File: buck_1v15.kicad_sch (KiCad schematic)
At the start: 20 parts, among them U2 TPS564257DRLR

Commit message: switch: buck v1.1 -> v1.15 as requested by the switch
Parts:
- renumbered C80 to C?, C72 to C?, C76 to C?, C73 to C?, C75 to C?, C71 to C?, C26 to C?, C79 to C?, C70 to C?, L2 to L?, R15 to R?, R84 to R?, R82 to R?, R16 to R?, R79 to R?, TP1 to TP?, TP10 to TP?, TP11 to TP?, TP3 to TP?, U2 to U?

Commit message: This commit intends to fix multiple issues:
 - 1.1 -> 1.15 v buck rails
 - Revision consistently using Rev. A
 - Issue with the Switch symbol when moving library
 - Adding new footprint and symbol for 2.54mm Headers
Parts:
- gave numbers to parts that had none: 20
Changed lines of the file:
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@@
 		(dnp no)
 		(fields_autoplaced yes)
-		(property "Reference" "#PWR?"
+		(property "Reference" "#PWR011"
 			(at 219.71 77.47 0)
 			(effects
@@
 		(dnp no)
 		(fields_autoplaced yes)
-		(property "Reference" "#PWR?"
+		(property "Reference" "#PWR015"
 			(at 85.09 107.95 0)
 			(effects
@@
 		(dnp no)
 		(fields_autoplaced yes)
-		(property "Reference" "TP?"
+		(property "Reference" "TP1"
 			(at 232.41 57.785 0)
 			(do_not_autoplace yes)
@@
 		(dnp yes)
 		(fields_autoplaced yes)
-		(property "Reference" "C?"
+		(property "Reference" "C80"
 			(at 88.9 92.7099 0)
 			(effects
@@
 		(on_board yes)
 		(dnp no)
-		(property "Reference" "R?"
+		(property "Reference" "R15"
 			(at 170.18 52.324 90)
 			(effects
@@
 		(dnp no)
 		(fields_autoplaced yes)
-		(property "Reference" "TP?"
+		(property "Reference" "TP10"
 			(at 166.624 67.31 90)
 			(do_not_autoplace yes)
@@
 		(dnp no)
 		(fields_autoplaced yes)
-		(property "Reference" "C?"
+		(property "Reference" "C72"
 			(at 241.3 66.0399 0)
 			(effects
@@
 		(dnp no)
 		(fields_autoplaced yes)
-		(property "Reference" "C?"
+		(property "Reference" "C76"
 			(at 93.98 72.3899 0)
 			(effects
@@
 		(dnp yes)
 		(fields_autoplaced yes)
-		(property "Reference" "C?"
+		(property "Reference" "C73"
 			(at 180.34 67.3099 0)
 			(effects
@@
 		(dnp yes)
 		(fields_autoplaced yes)
-		(property "Reference" "C?"
+		(property "Reference" "C75"
 			(at 82.55 72.3899 0)
 			(effects
@@
 		(dnp no)
 		(fields_autoplaced yes)
-		(property "Reference" "L?"
+		(property "Reference" "L2"
 			(at 170.18 61.722 0)
 			(do_not_autoplace yes)
@@
 		(dnp yes)
 		(fields_autoplaced yes)
-		(property "Reference" "R?"
+		(property "Reference" "R84"
 			(at 99.06 92.7099 0)
 			(effects
@@
 		(dnp no)
 		(fields_autoplaced yes)
-		(property "Reference" "R?"
+		(property "Reference" "R82"
 			(at 190.5 81.2799 0)
 			(effects
@@
 		(dnp no)
 		(fields_autoplaced yes)
-		(property "Reference" "C?"
+		(property "Reference" "C71"
 			(at 229.87 66.0399 0)
 			(effects
@@
 		(dnp yes)
 		(fields_autoplaced yes)
-		(property "Reference" "C?"
+		(property "Reference" "C26"
 			(at 207.01 66.0399 0)
 			(effects
@@
 		(dnp no)
 		(fields_autoplaced yes)
-		(property "Reference" "C?"
+		(property "Reference" "C79"
 			(at 105.41 72.3899 0)
 			(effects
@@
 		(on_board yes)
 		(dnp no)
-		(property "Reference" "R?"
+		(property "Reference" "R16"
 			(at 64.77 63.5 90)
 			(effects
@@
 		(dnp no)
 		(fields_autoplaced yes)
-		(property "Reference" "R?"
+		(property "Reference" "R79"
 			(at 190.5 67.3099 0)
 			(effects
@@
 		(dnp no)
 		(fields_autoplaced yes)
-		(property "Reference" "#PWR?"
+		(property "Reference" "#PWR014"
 			(at 187.96 96.52 0)
 			(effects
@@
 		(dnp no)
 		(fields_autoplaced yes)
-		(property "Reference" "TP?"
+		(property "Reference" "TP11"
 			(at 96.52 84.455 0)
 			(do_not_autoplace yes)
@@
 		(dnp no)
 		(fields_autoplaced yes)
-		(property "Reference" "#PWR?"
+		(property "Reference" "#PWR010"
 			(at 214.63 64.77 0)
 			(effects
@@
 		(dnp no)
 		(fields_autoplaced yes)
-		(property "Reference" "#PWR?"
+		(property "Reference" "#PWR012"
 			(at 154.94 82.55 0)
 			(effects
@@
 		(dnp no)
 		(fields_autoplaced yes)
-		(property "Reference" "C?"
+		(property "Reference" "C70"
 			(at 218.44 66.0399 0)
 			(effects
@@
 		(dnp no)
 		(fields_autoplaced yes)
-		(property "Reference" "TP?"
+		(property "Reference" "TP3"
 			(at 71.12 60.325 0)
 			(do_not_autoplace yes)
@@
 		(dnp no)
 		(fields_autoplaced yes)
-		(property "Reference" "#PWR?"
+		(property "Reference" "#PWR013"
 			(at 90.17 85.09 0)
 			(effects
@@
 		(dnp no)
 		(fields_autoplaced yes)
-		(property "Reference" "#PWR?"
+		(property "Reference" "#PWR023"
 			(at 48.26 53.34 0)
 			(effects
@@
 		(dnp no)
 		(fields_autoplaced yes)
-		(property "Reference" "U?"
+		(property "Reference" "U2"
 			(at 134.62 55.88 0)
 			(effects
@@
 		(dnp no)
 		(fields_autoplaced yes)
-		(property "Reference" "#PWR?"
+		(property "Reference" "#PWR022"
 			(at 48.26 38.1 0)
 			(effects

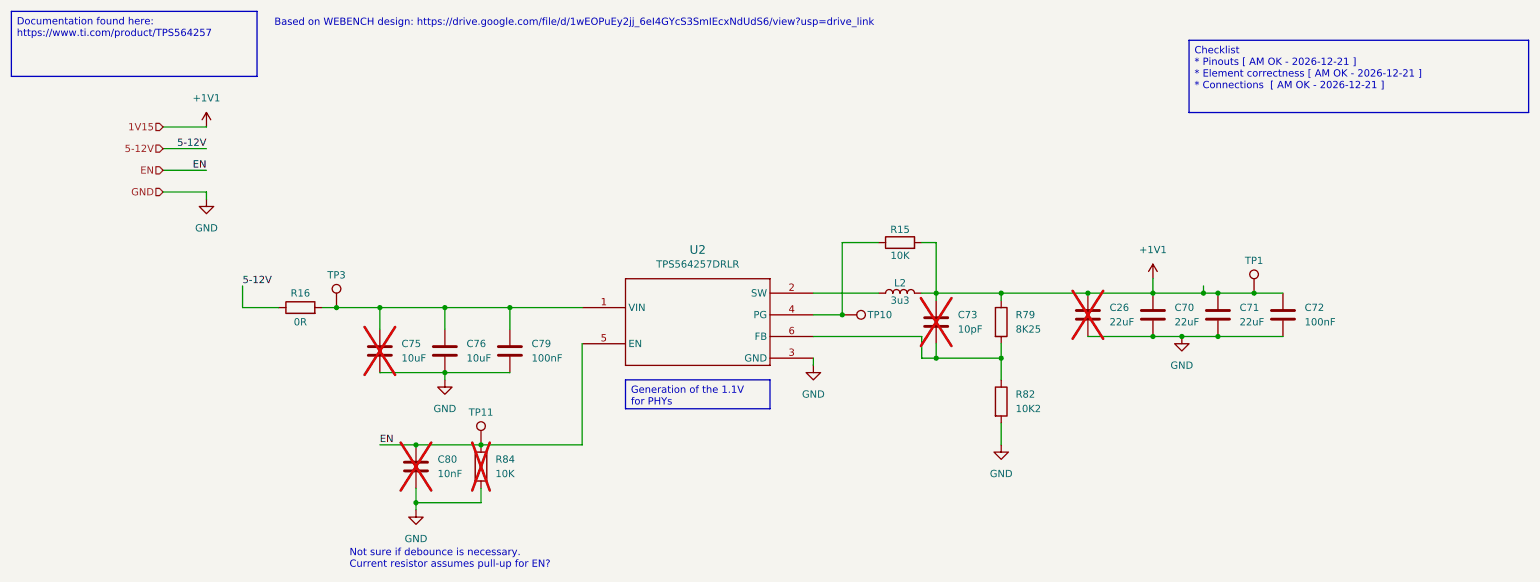
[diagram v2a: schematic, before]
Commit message: fixing issue related to symbol changes, and updating components
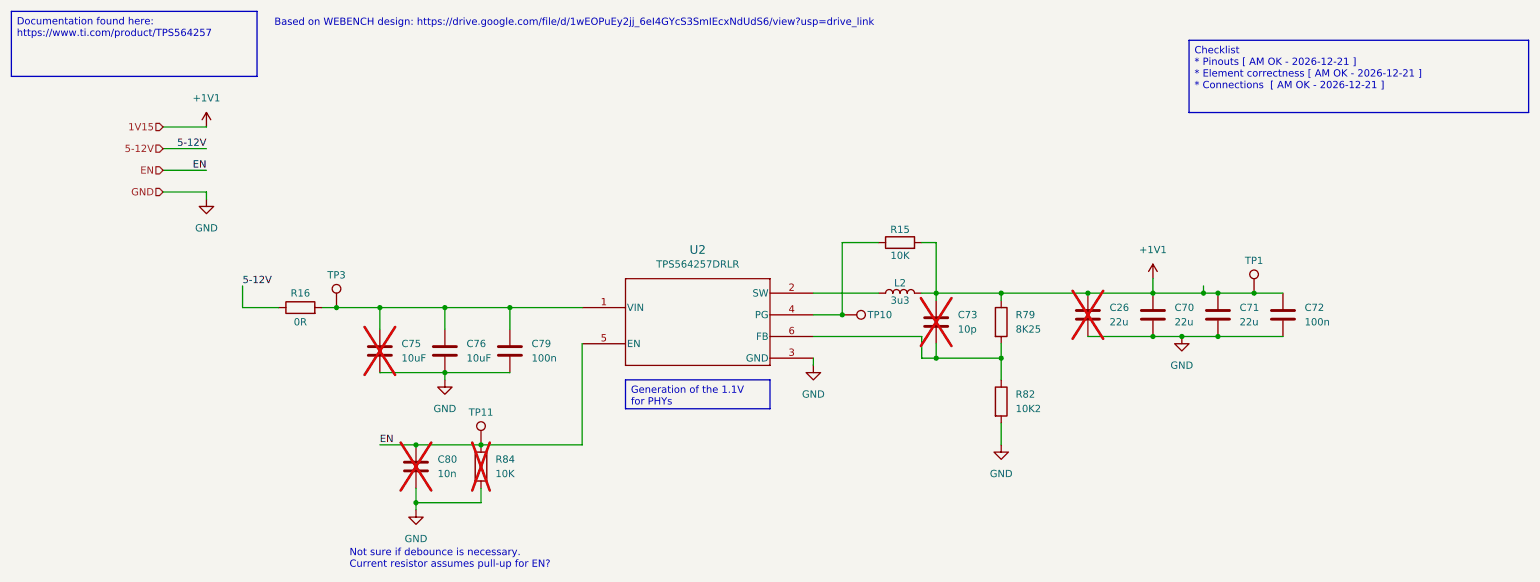
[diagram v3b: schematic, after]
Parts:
- C26, C70, C71: value 22uF -> 22u; symbol KL_C:C_22uF_10V_X5R_0603_20 -> KL_C:C_22u_10V_X5R_0603_20; Digikey 490-10476-1-ND -> 490-13243-1-ND; LCSC C84419 -> C361061; Mouser 81-GRM188R61A226ME5D -> 81-GRM187R61A226ME5D
- C72: value 100nF -> 100n; footprint KL:C_0603 -> Capacitor_SMD:C_0201_0603Metric; symbol KL_C:C_100nF_10V_X7R_0603_10 -> KL_C:C_100n_10V_X7R_0603_10
- C73: value 10pF -> 10p; symbol KL_C:C_10pF_25V_C0G_0603_5 -> KL_C:C_10p_25V_C0G_0603_5
- C75, C76: footprint KL:C_0603 -> Capacitor_SMD:C_0201_0603Metric; symbol KL_C:C_10uF_25V_X5R_0603_20 -> KL_C:C_10u_25V_X5R_0603_20
- C79: value 100nF -> 100n; footprint KL:C_0603 -> Capacitor_SMD:C_0201_0603Metric; symbol KL_C:C_100nF_16V_X7R_0603_10 -> KL_C:C_100n_16V_X7R_0603_10
- C80: value 10nF -> 10n; footprint KL:C_0603 -> Capacitor_SMD:C_0201_0603Metric; symbol KL_C:C_10nF_25V_X7R_0603_20 -> KL_C:C_10n_50V_X7R_0603_10; Digikey 311-3111-1-ND -> 1276-CL10B103KB8WPNDCT-ND; LCSC C726559 -> C307346; Mouser 603-AC603KRX7R8BB103 -> 187-CL10B103KB8WPND; Tolerance 20 -> 10; Voltage 25 -> 50; now in the parts list
- R82, R84: footprint KL:R_0603 -> KL_Footprints:C_0603
- U2: footprint KL:SOT-563 -> KL_Footprints:SOT-563; symbol KL_IC_Power:TI_TPS564357DRLR -> KL_Voltage_Regulators:TPS564257DRLR; LCSC (none) -> C19272233; Mouser 595-TPS564257DRLR -> 595-TPS564257DRLR
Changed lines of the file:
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@@
 		(dnp no)
 		(fields_autoplaced yes)
-		(property "Reference" "#PWR011"
+		(property "Reference" "#PWR11"
 			(at 219.71 77.47 0)
 			(effects
@@
 			(project "shish-lan"
 				(path "/d4536448-b109-4159-96e2-3dc21baf2d6e/0b7d9af9-83c1-43fa-a7a0-a33d0a00ea9c/42c65065-b6e5-43b0-ae2c-34333f058269"
-					(reference "#PWR011")
+					(reference "#PWR11")
 					(unit 1)
 				)
@@
 		(dnp no)
 		(fields_autoplaced yes)
-		(property "Reference" "#PWR015"
+		(property "Reference" "#PWR15"
 			(at 85.09 107.95 0)
 			(effects
@@
 			(project "shish-lan"
 				(path "/d4536448-b109-4159-96e2-3dc21baf2d6e/0b7d9af9-83c1-43fa-a7a0-a33d0a00ea9c/42c65065-b6e5-43b0-ae2c-34333f058269"
-					(reference "#PWR015")
+					(reference "#PWR15")
 					(unit 1)
 				)
@@
 	)
 	(symbol
-		(lib_id "KL_C:C_10nF_25V_X7R_0603_20")
+		(lib_id "KL_C:C_10n_50V_X7R_0603_10")
 		(at 85.09 93.98 0)
 		(unit 1)
 		(exclude_from_sim no)
-		(in_bom no)
+		(in_bom yes)
 		(on_board yes)
 		(dnp yes)
@@
 			)
 		)
-		(property "Value" "10nF"
+		(property "Value" "10n"
 			(at 88.9 95.2499 0)
 			(effects
@@
 			)
 		)
-		(property "Footprint" "KL:C_0603"
+		(property "Footprint" "Capacitor_SMD:C_0201_0603Metric"
 			(at 86.0552 97.79 0)
 			(effects
@@
 			)
 		)
-		(property "Tolerance" "20"
+		(property "Tolerance" "10"
 			(at 85.09 93.98 0)
 			(effects
@@
 			)
 		)
-		(property "Voltage" "25"
+		(property "Voltage" "50"
 			(at 85.09 93.98 0)
 			(effects
@@
 			)
 		)
-		(property "Mouser" "603-AC603KRX7R8BB103"
+		(property "Mouser" "187-CL10B103KB8WPND"
 			(at 85.09 93.98 0)
 			(effects
@@
 			)
 		)
-		(property "Digikey" "311-3111-1-ND"
+		(property "Digikey" "1276-CL10B103KB8WPNDCT-ND"
 			(at 85.09 93.98 0)
 			(effects
@@
 			)
 		)
-		(property "LCSC" "C726559"
+		(property "LCSC" "C307346"
 			(at 85.09 93.98 0)
 			(effects
@@
 	)
 	(symbol
-		(lib_name "R_10K_100mW_5_0603_1")
 		(lib_id "KL_R:R_10K_100mW_5_0603")
 		(at 170.18 54.61 90)
@@
 	)
 	(symbol
-		(lib_id "KL_C:C_100nF_10V_X7R_0603_10")
+		(lib_id "KL_C:C_100n_10V_X7R_0603_10")
 		(at 237.49 67.31 0)
 		(unit 1)
@@
 			)
 		)
-		(property "Value" "100nF"
+		(property "Value" "100n"
 			(at 241.3 68.5799 0)
 			(effects
@@
 			)
 		)
-		(property "Footprint" "KL:C_0603"
+		(property "Footprint" "Capacitor_SMD:C_0201_0603Metric"
 			(at 238.4552 71.12 0)
 			(effects
@@
 	)
 	(symbol
-		(lib_id "KL_C:C_10uF_25V_X5R_0603_20")
+		(lib_id "KL_C:C_10u_25V_X5R_0603_20")
 		(at 90.17 73.66 0)
 		(unit 1)
@@
 			)
 		)
-		(property "Footprint" "KL:C_0603"
+		(property "Footprint" "Capacitor_SMD:C_0201_0603Metric"
 			(at 91.1352 77.47 0)
 			(effects
@@
 	)
 	(symbol
-		(lib_id "KL_C:C_10pF_25V_C0G_0603_5")
+		(lib_id "KL_C:C_10p_25V_C0G_0603_5")
 		(at 176.53 68.58 0)
 		(unit 1)
@@
 			)
 		)
-		(property "Value" "10pF"
+		(property "Value" "10p"
 			(at 180.34 69.8499 0)
 			(effects
@@
 	)
 	(symbol
-		(lib_id "KL_C:C_10uF_25V_X5R_0603_20")
+		(lib_id "KL_C:C_10u_25V_X5R_0603_20")
 		(at 78.74 73.66 0)
 		(unit 1)
@@
 			)
 		)
-		(property "Footprint" "KL:C_0603"
+		(property "Footprint" "Capacitor_SMD:C_0201_0603Metric"
 			(at 79.7052 77.47 0)
 			(effects
@@
 			)
 		)
-		(property "Footprint" "KL:R_0603"
+		(property "Footprint" "KL_Footprints:C_0603"
 			(at 94.742 93.98 90)
 			(effects
@@
 			)
 		)
-		(property "Footprint" "KL:R_0603"
+		(property "Footprint" "KL_Footprints:C_0603"
 			(at 186.182 82.55 90)
 			(effects
@@
 	)
 	(symbol
-		(lib_id "KL_C:C_22uF_10V_X5R_0603_20")
+		(lib_id "KL_C:C_22u_10V_X5R_0603_20")
 		(at 226.06 67.31 0)
 		(unit 1)
@@
 			)
 		)
-		(property "Value" "22uF"
+		(property "Value" "22u"
 			(at 229.87 68.5799 0)
 			(effects
@@
 			)
 		)
-		(property "Mouser" "81-GRM188R61A226ME5D"
+		(property "Mouser" "81-GRM187R61A226ME5D"
 			(at 226.06 67.31 0)
 			(effects
@@
 			)
 		)
-		(property "Digikey" "490-10476-1-ND"
+		(property "Digikey" "490-13243-1-ND"
 			(at 226.06 67.31 0)
 			(effects
@@
 			)
 		)
-		(property "LCSC" "C84419"
+		(property "LCSC" "C361061"
 			(at 226.06 67.31 0)
 			(effects
@@
 	)
 	(symbol
-		(lib_id "KL_C:C_22uF_10V_X5R_0603_20")
+		(lib_id "KL_C:C_22u_10V_X5R_0603_20")
 		(at 203.2 67.31 0)
 		(unit 1)
@@
 			)
 		)
-		(property "Value" "22uF"
+		(property "Value" "22u"
 			(at 207.01 68.5799 0)
 			(effects
@@
 			)
 		)
-		(property "Mouser" "81-GRM188R61A226ME5D"
+		(property "Mouser" "81-GRM187R61A226ME5D"
 			(at 203.2 67.31 0)
 			(effects
@@
 			)
 		)
-		(property "Digikey" "490-10476-1-ND"
+		(property "Digikey" "490-13243-1-ND"
 			(at 203.2 67.31 0)
 			(effects
@@
 			)
 		)
-		(property "LCSC" "C84419"
+		(property "LCSC" "C361061"
 			(at 203.2 67.31 0)
 			(effects
@@
 	)
 	(symbol
-		(lib_id "KL_C:C_100nF_16V_X7R_0603_10")
+		(lib_id "KL_C:C_100n_16V_X7R_0603_10")
 		(at 101.6 73.66 0)
 		(unit 1)
@@
 			)
 		)
-		(property "Value" "100nF"
+		(property "Value" "100n"
 			(at 105.41 74.9299 0)
 			(effects
@@
 			)
 		)
-		(property "Footprint" "KL:C_0603"
+		(property "Footprint" "Capacitor_SMD:C_0201_0603Metric"
 			(at 102.5652 77.47 0)
 			(effects
@@
 		(dnp no)
 		(fields_autoplaced yes)
-		(property "Reference" "#PWR014"
+		(property "Reference" "#PWR14"
 			(at 187.96 96.52 0)
 			(effects
@@
 			(project "shish-lan"
 				(path "/d4536448-b109-4159-96e2-3dc21baf2d6e/0b7d9af9-83c1-43fa-a7a0-a33d0a00ea9c/42c65065-b6e5-43b0-ae2c-34333f058269"
-					(reference "#PWR014")
+					(reference "#PWR14")
 					(unit 1)
 				)
@@
 		(dnp no)
 		(fields_autoplaced yes)
-		(property "Reference" "#PWR010"
+		(property "Reference" "#PWR10"
 			(at 214.63 64.77 0)
 			(effects
@@
 			(project ""
 				(path "/d4536448-b109-4159-96e2-3dc21baf2d6e/0b7d9af9-83c1-43fa-a7a0-a33d0a00ea9c/42c65065-b6e5-43b0-ae2c-34333f058269"
-					(reference "#PWR010")
+					(reference "#PWR10")
 					(unit 1)
 				)
@@
 		(dnp no)
 		(fields_autoplaced yes)
-		(property "Reference" "#PWR012"
+		(property "Reference" "#PWR12"
 			(at 154.94 82.55 0)
 			(effects
@@
 			(project "shish-lan"
 				(path "/d4536448-b109-4159-96e2-3dc21baf2d6e/0b7d9af9-83c1-43fa-a7a0-a33d0a00ea9c/42c65065-b6e5-43b0-ae2c-34333f058269"
-					(reference "#PWR012")
+					(reference "#PWR12")
 					(unit 1)
 				)
@@
 	)
 	(symbol
-		(lib_id "KL_C:C_22uF_10V_X5R_0603_20")
+		(lib_id "KL_C:C_22u_10V_X5R_0603_20")
 		(at 214.63 67.31 0)
 		(unit 1)
@@
 			)
 		)
-		(property "Value" "22uF"
+		(property "Value" "22u"
 			(at 218.44 68.5799 0)
 			(effects
@@
 			)
 		)
-		(property "Mouser" "81-GRM188R61A226ME5D"
+		(property "Mouser" "81-GRM187R61A226ME5D"
 			(at 214.63 67.31 0)
 			(effects
@@
 			)
 		)
-		(property "Digikey" "490-10476-1-ND"
+		(property "Digikey" "490-13243-1-ND"
 			(at 214.63 67.31 0)
 			(effects
@@
 			)
 		)
-		(property "LCSC" "C84419"
+		(property "LCSC" "C361061"
 			(at 214.63 67.31 0)
 			(effects
@@
 		(dnp no)
 		(fields_autoplaced yes)
-		(property "Reference" "#PWR013"
+		(property "Reference" "#PWR13"
 			(at 90.17 85.09 0)
 			(effects
@@
 			(project "shish-lan"
 				(path "/d4536448-b109-4159-96e2-3dc21baf2d6e/0b7d9af9-83c1-43fa-a7a0-a33d0a00ea9c/42c65065-b6e5-43b0-ae2c-34333f058269"
-					(reference "#PWR013")
+					(reference "#PWR13")
 					(unit 1)
 				)
@@
 		(dnp no)
 		(fields_autoplaced yes)
-		(property "Reference" "#PWR023"
+		(property "Reference" "#PWR23"
 			(at 48.26 53.34 0)
 			(effects
@@
 			(project ""
 				(path "/d4536448-b109-4159-96e2-3dc21baf2d6e/0b7d9af9-83c1-43fa-a7a0-a33d0a00ea9c/42c65065-b6e5-43b0-ae2c-34333f058269"
-					(reference "#PWR023")
+					(reference "#PWR23")
 					(unit 1)
 				)
@@
 	)
 	(symbol
-		(lib_id "KL_IC_Power:TI_TPS564357DRLR")
-		(at 134.62 68.58 0)
+		(lib_id "KL_Voltage_Regulators:TPS564257DRLR")
+		(at 114.3 66.04 0)
 		(unit 1)
 		(exclude_from_sim no)
@@
 			)
 		)
-		(property "Footprint" "KL:SOT-563"
-			(at 134.62 63.5 0)
-			(effects
-				(font
-					(size 1.27 1.27)
-				)
-				(hide yes)
-			)
-		)
-		(property "Datasheet" ""
-			(at 134.62 63.5 0)
-			(effects
-				(font
-					(size 1.27 1.27)
+		(property "Footprint" "KL_Footprints:SOT-563"
+			(at 114.3 66.04 0)
+			(effects
+				(font
+					(size 1.27 1.27)
+					(italic yes)
+				)
+				(hide yes)
+			)
+		)
+		(property "Datasheet" "https://www.ti.com/lit/gpn/tps564257"
+			(at 114.3 66.04 0)
+			(effects
+				(font
+					(size 1.27 1.27)
+					(italic yes)
 				)
 				(hide yes)
@@
 		)
 		(property "Description" ""
-			(at 134.62 63.5 0)
-			(effects
-				(font
-					(size 1.27 1.27)
-				)
-				(hide yes)
-			)
-		)
-		(property "Mouser" "595-TPS564257DRLR"
-			(at 134.62 68.58 0)
+			(at 114.3 66.04 0)
+			(effects
+				(font
+					(size 1.27 1.27)
+				)
+				(hide yes)
+			)
+		)
+		(property "Mouser" " 595-TPS564257DRLR "
+			(at 114.3 66.04 0)
 			(effects
 				(font
@@
 		)
 		(property "Digikey" "296-TPS564257DRLRCT-ND"
-			(at 134.62 68.58 0)
+			(at 114.3 66.04 0)
 			(effects
 				(font
@@
 		)
 		(property "LSCS" "C19272233"
-			(at 134.62 68.58 0)
+			(at 114.3 66.04 0)
+			(effects
+				(font
+					(size 1.27 1.27)
+				)
+				(hide yes)
+			)
+		)
+		(property "LCSC" "C19272233"
+			(at 114.3 66.04 0)
 			(effects
 				(font
@@
 		(dnp no)
 		(fields_autoplaced yes)
-		(property "Reference" "#PWR022"
+		(property "Reference" "#PWR22"
 			(at 48.26 38.1 0)
 			(effects
@@
 			(project ""
 				(path "/d4536448-b109-4159-96e2-3dc21baf2d6e/0b7d9af9-83c1-43fa-a7a0-a33d0a00ea9c/42c65065-b6e5-43b0-ae2c-34333f058269"
-					(reference "#PWR022")
-					(unit 1)
-				)
+					(reference "#PWR22")
+					(unit 1)
+				)

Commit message: updates all symbols to the project only paths. My bad - sorry
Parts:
- C26, C73, C75, R84: now in the parts list
- U2: LSCS C19272233 -> (none)
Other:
- moved on the sheet: TP10
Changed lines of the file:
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@@
 	)
 	(junction
-		(at 160.02 67.31)
+		(at 214.63 63.5)
 		(diameter 0)
 		(color 0 0 0 0)
 	)
 	(junction
-		(at 214.63 63.5)
+		(at 78.74 66.04)
 		(diameter 0)
 		(color 0 0 0 0)
 	)
 	(junction
-		(at 78.74 66.04)
+		(at 161.29 54.61)
 		(diameter 0)
 		(color 0 0 0 0)
@@
 	(wire
 		(pts
+			(xy 161.29 54.61) (xy 160.02 54.61)
+		)
+		(stroke
+			(width 0)
+			(type default)
+		)
+	)
+	(wire
+		(pts
 			(xy 173.99 63.5) (xy 176.53 63.5)
 		)
@@
 	(wire
 		(pts
-			(xy 166.37 54.61) (xy 160.02 54.61)
+			(xy 166.37 54.61) (xy 161.29 54.61)
 		)
 		(stroke
@@
 		(on_board yes)
 		(dnp no)
+		(fields_autoplaced yes)
 		(property "Reference" "R15"
-			(at 170.18 52.324 90)
+			(at 170.18 48.26 90)
 			(effects
 				(font
@@
 		)
 		(property "Value" "10K"
-			(at 170.18 56.896 90)
+			(at 170.18 50.8 90)
 			(effects
 				(font
@@
 	(symbol
 		(lib_id "KL_TP:TestPoint")
-		(at 160.02 67.31 270)
+		(at 161.29 54.61 0)
 		(unit 1)
 		(exclude_from_sim no)
@@
 		(fields_autoplaced yes)
 		(property "Reference" "TP10"
-			(at 166.624 67.31 90)
+			(at 161.29 48.895 0)
 			(do_not_autoplace yes)
 			(effects
@@
 		)
 		(property "Value" "~"
-			(at 165.1 67.31 0)
+			(at 161.29 49.53 0)
 			(effects
 				(font
@@
 		)
 		(property "Footprint" "Connector_PinHeader_2.54mm:PinHeader_1x01_P2.54mm_Vertical"
-			(at 160.02 72.39 0)
+			(at 166.37 54.61 0)
 			(effects
 				(font
@@
 		)
 		(property "Datasheet" "~"
-			(at 160.02 72.39 0)
+			(at 166.37 54.61 0)
 			(effects
 				(font
@@
 		)
 		(property "Description" "test point"
-			(at 160.02 67.31 0)
+			(at 161.29 54.61 0)
 			(effects
 				(font
@@
 		(unit 1)
 		(exclude_from_sim no)
-		(in_bom no)
+		(in_bom yes)
 		(on_board yes)
 		(dnp yes)
@@
 		(unit 1)
 		(exclude_from_sim no)
-		(in_bom no)
+		(in_bom yes)
 		(on_board yes)
 		(dnp yes)
@@
 		(unit 1)
 		(exclude_from_sim no)
-		(in_bom no)
+		(in_bom yes)
 		(on_board yes)
 		(dnp yes)
@@
 		(unit 1)
 		(exclude_from_sim no)
-		(in_bom no)
+		(in_bom yes)
 		(on_board yes)
 		(dnp yes)
@@
 		(on_board yes)
 		(dnp no)
+		(fields_autoplaced yes)
 		(property "Reference" "R16"
-			(at 64.77 63.5 90)
+			(at 64.77 59.69 90)
 			(effects
 				(font
@@
 		)
 		(property "Value" "0R"
-			(at 64.77 68.58 90)
+			(at 64.77 62.23 90)
 			(effects
 				(font
@@
 			(effects
 				(font
-					(size 1.27 1.27)
+					(size 1.524 1.524)
 				)
 			)
@@
 			(at 114.3 66.04 0)
 			(effects
-				(font
-					(size 1.27 1.27)
-				)
-				(hide yes)
-			)
-		)
-		(property "LSCS" "C19272233"
-			(at 114.3 66.04 0)
-			(effects
